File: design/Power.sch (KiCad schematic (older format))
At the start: 48 parts, among them U1 DRV8302, U2 TC2117

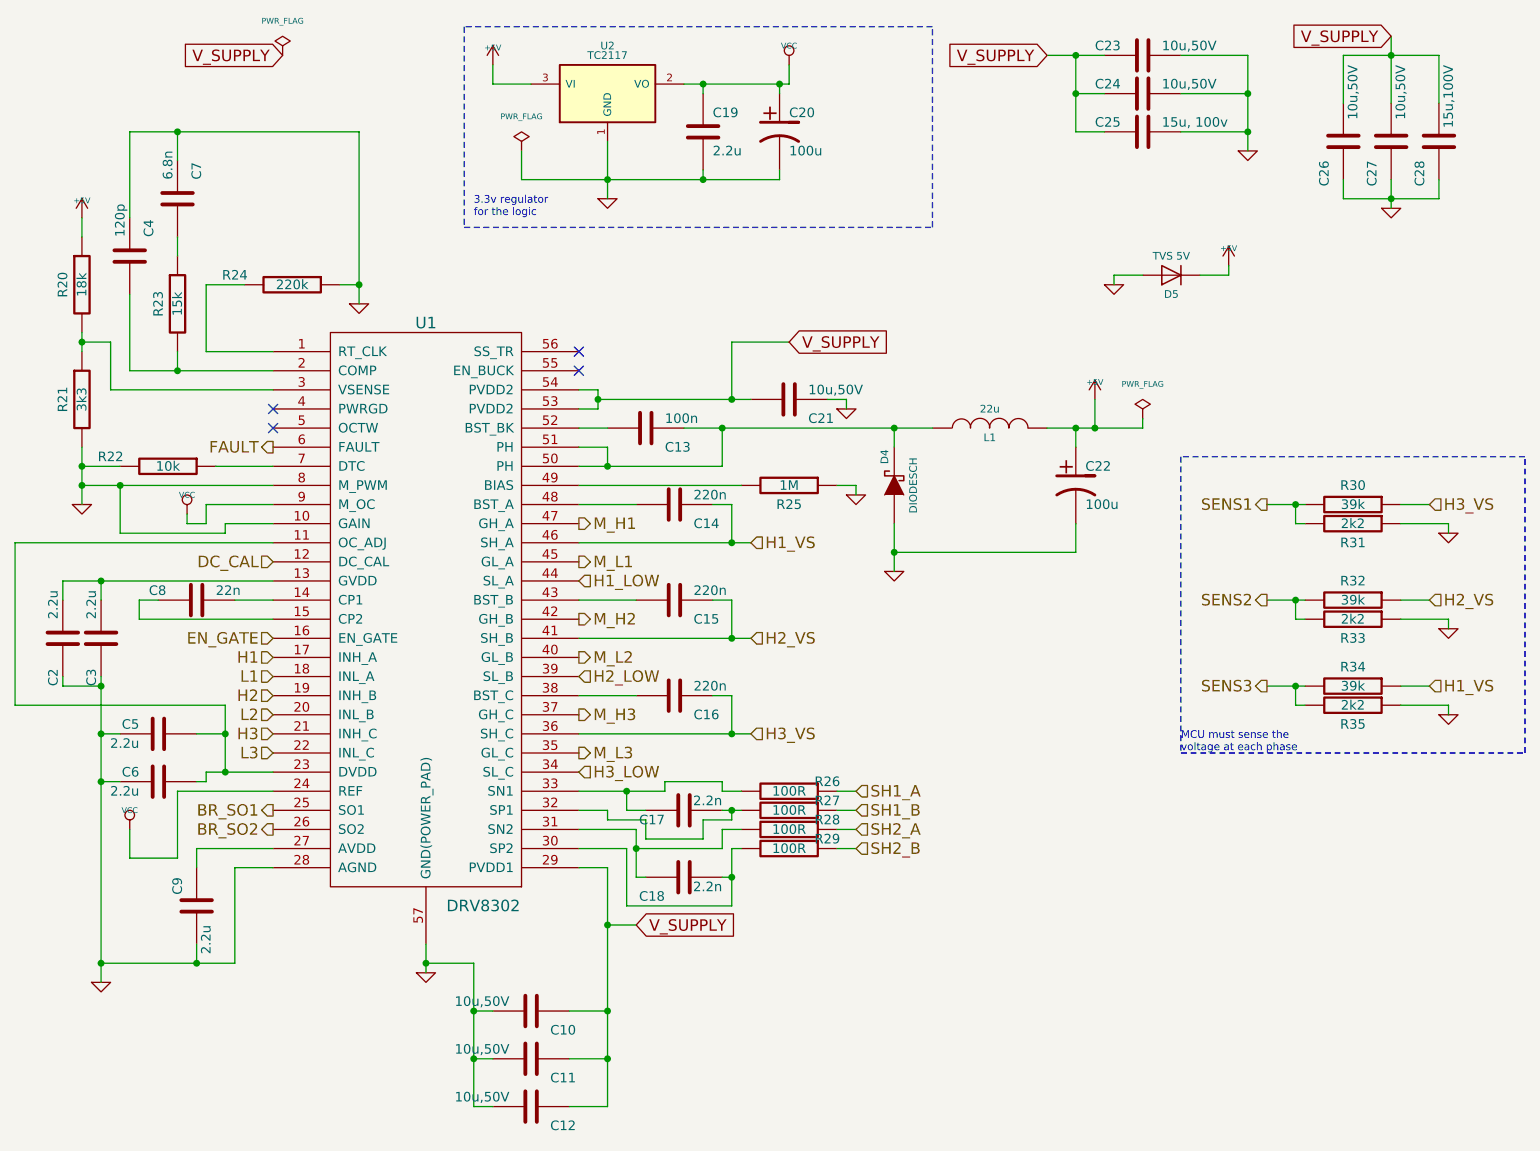
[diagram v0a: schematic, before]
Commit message: Added BOM and reworked component naming to be inline with old VESC names
:^)
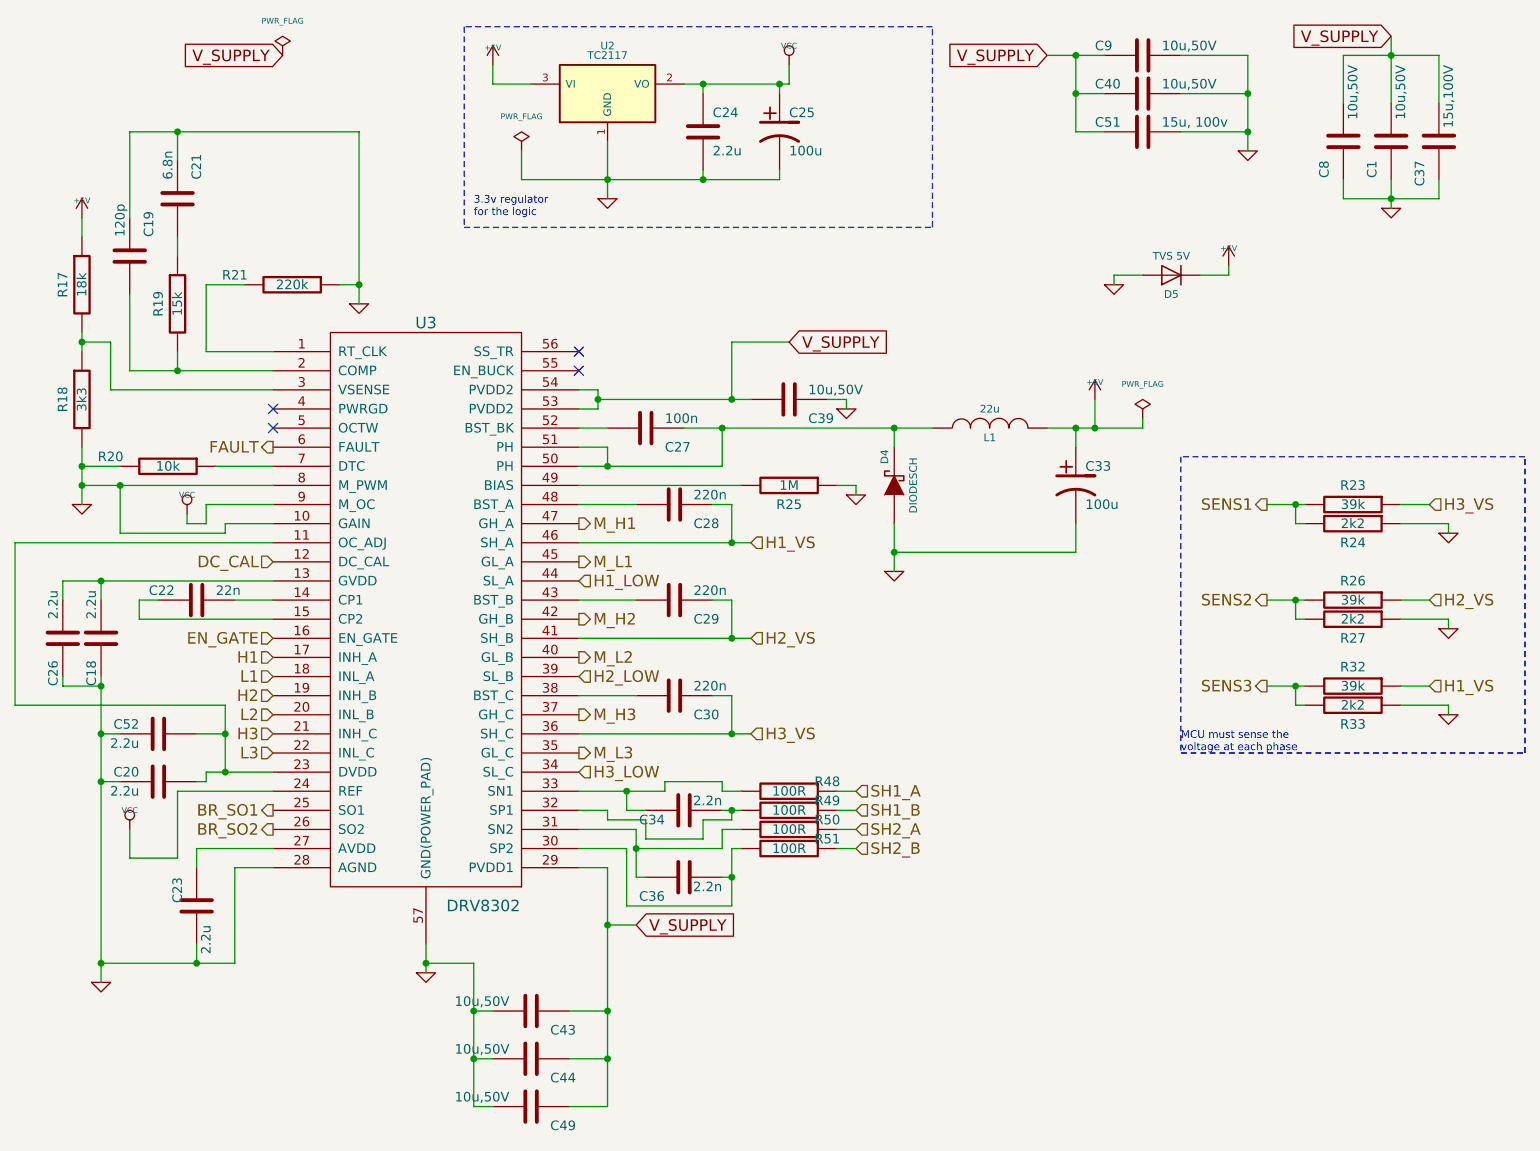
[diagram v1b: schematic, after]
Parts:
- renumbered C27 to C1, C3 to C18, C4 to C19, C6 to C20, C7 to C21, C8 to C22, C9 to C23, C19 to C24, C20 to C25, C2 to C26, C13 to C27, C14 to C28, C15 to C29, C16 to C30, C22 to C33, C17 to C34, C18 to C36, C28 to C37, C21 to C39, C24 to C40, C10 to C43, C11 to C44, C12 to C49, C25 to C51, C5 to C52, C26 to C8, C23 to C9, R20 to R17, R21 to R18, R23 to R19, R22 to R20, R24 to R21, R30 to R23, R31 to R24, R32 to R26, R33 to R27, R34 to R32, R35 to R33, R26 to R48, R27 to R49, R28 to R50, R29 to R51, U1 to U3
